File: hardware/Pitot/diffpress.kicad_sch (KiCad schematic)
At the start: 6 parts, among them IC1 ABPMRRV060MG2A3

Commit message: small changes, cubemx needs checking
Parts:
- added R18: 4.7k, Resistor_SMD:R_0603_1608Metric_Pad0.98x0.95mm_HandSolder, symbol Device:R
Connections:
- net GND: now also R18.2
- net pressureERR: now also R18.1
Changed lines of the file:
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@@
 	(paper "A4")
+	(junction
+		(at 90.17 58.42)
+		(diameter 0)
+		(color 0 0 0 0)
+	)
 	(junction
 		(at 101.6 74.93)
@@
 	(wire
 		(pts
+			(xy 90.17 58.42) (xy 90.17 62.23)
+		)
+		(stroke
+			(width 0)
+			(type default)
+		)
+	)
+	(wire
+		(pts
 			(xy 166.37 66.04) (xy 166.37 69.85)
 		)
@@
 	(wire
 		(pts
-			(xy 96.52 58.42) (xy 115.57 58.42)
+			(xy 90.17 58.42) (xy 115.57 58.42)
+		)
+		(stroke
+			(width 0)
+			(type default)
+		)
+	)
+	(wire
+		(pts
+			(xy 81.28 58.42) (xy 90.17 58.42)
 		)
 		(stroke
@@
 		(pts
 			(xy 151.13 69.85) (xy 166.37 69.85)
+		)
+		(stroke
+			(width 0)
+			(type default)
+		)
+	)
+	(wire
+		(pts
+			(xy 90.17 69.85) (xy 90.17 73.66)
 		)
 		(stroke
@@
 	(hierarchical_label "pressureERR"
 		(shape output)
-		(at 96.52 58.42 180)
+		(at 81.28 58.42 180)
 		(effects
 			(font
@@
 					(unit 1)
 				)
+			)
+		)
+	)
+	(symbol
+		(lib_id "power:GND")
+		(at 90.17 73.66 0)
+		(unit 1)
+		(exclude_from_sim no)
+		(in_bom yes)
+		(on_board yes)
+		(dnp no)
+		(property "Reference" "#PWR030"
+			(at 90.17 80.01 0)
+			(effects
+				(font
+					(size 1.27 1.27)
+				)
+				(hide yes)
+			)
+		)
+		(property "Value" "GND"
+			(at 90.17 77.724 0)
+			(effects
+				(font
+					(size 1.27 1.27)
+				)
+			)
+		)
+		(property "Footprint" ""
+			(at 90.17 73.66 0)
+			(effects
+				(font
+					(size 1.27 1.27)
+				)
+				(hide yes)
+			)
+		)
+		(property "Datasheet" ""
+			(at 90.17 73.66 0)
+			(effects
+				(font
+					(size 1.27 1.27)
+				)
+				(hide yes)
+			)
+		)
+		(property "Description" "Power symbol creates a global label with name \"GND\" , ground"
+			(at 90.17 73.66 0)
+			(effects
+				(font
+					(size 1.27 1.27)
+				)
+				(hide yes)
+			)
+		)
+		(pin "1"
+		)
+		(instances
+			(project "Pitot"
+				(path "/b92f2323-f48d-45bc-8bf4-2cff87ecc0bc/1905abd7-6f86-4e5e-9f35-1efc7ddf21d8"
+					(reference "#PWR031")
+					(unit 1)
+				)
+				(path "/b92f2323-f48d-45bc-8bf4-2cff87ecc0bc/5b12aa57-1644-4b30-a37a-ee43545972bc"
+					(reference "#PWR030")
+					(unit 1)
+				)
+			)
+		)
+	)
+	(symbol
+		(lib_id "Device:R")
+		(at 90.17 66.04 0)
+		(unit 1)
+		(exclude_from_sim no)
+		(in_bom yes)
+		(on_board yes)
+		(dnp yes)
+		(property "Reference" "R18"
+			(at 92.202 65.2779 0)
+			(effects
+				(font
+					(size 1.27 1.27)
+				)
+				(justify left)
+			)
+		)
+		(property "Value" "4.7k"
+			(at 92.202 67.564 0)
+			(effects
+				(font
+					(size 1.27 1.27)
+				)
+				(justify left)
+			)
+		)
+		(property "Footprint" "Resistor_SMD:R_0603_1608Metric_Pad0.98x0.95mm_HandSolder"
+			(at 88.392 66.04 90)
+			(effects
+				(font
+					(size 1.27 1.27)
+				)
+				(hide yes)
+			)
+		)
+		(property "Datasheet" "~"
+			(at 90.17 66.04 0)
+			(effects
+				(font
+					(size 1.27 1.27)
+				)
+				(hide yes)
+			)
+		)
+		(property "Description" "Resistor"
+			(at 90.17 66.04 0)
+			(effects
+				(font
+					(size 1.27 1.27)
+				)
+				(hide yes)
+			)
+		)
+		(property "P/N" "71-CRCW0603-4.7K-E3"
+			(at 90.17 66.04 0)
+			(effects
+				(font
+					(size 1.27 1.27)
+				)
+				(hide yes)
+			)
+		)
+		(pin "2"
+		)
+		(pin "1"
+		)
+		(instances
+			(project "Pitot"
+				(path "/b92f2323-f48d-45bc-8bf4-2cff87ecc0bc/1905abd7-6f86-4e5e-9f35-1efc7ddf21d8"
+					(reference "R19")
+					(unit 1)
+				)
+				(path "/b92f2323-f48d-45bc-8bf4-2cff87ecc0bc/5b12aa57-1644-4b30-a37a-ee43545972bc"
+					(reference "R18")
+					(unit 1)
+				)

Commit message: finished layout
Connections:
- net +3.3VMCU is gone; now on net +3.3V: C5.1, C6.1, IC1.2 (VSUPPLY)
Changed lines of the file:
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@@
 			)
 		)
-		(property "Value" "+3.3VMCU"
+		(property "Value" "+3.3V"
 			(at 101.6 60.452 0)
 			(effects

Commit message: final pitot board + bom files
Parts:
- IC1: P/N 785-ABPMRRV060MG2A3 -> ABPMRRV060MG2A3
- R10, R11, R18, R9: P/N 71-CRCW0603-4.7K-E3 -> CRCW06034K70FKEA
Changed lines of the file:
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@@
 			)
 		)
-		(property "P/N" "71-CRCW0603-4.7K-E3"
+		(property "P/N" "CRCW06034K70FKEA"
 			(at 115.57 53.34 0)
 			(effects
@@
 			)
 		)
-		(property "P/N" "71-CRCW0603-4.7K-E3"
+		(property "P/N" "CRCW06034K70FKEA"
 			(at 166.37 62.23 0)
 			(effects
@@
 			)
 		)
-		(property "P/N" "71-CRCW0603-4.7K-E3"
+		(property "P/N" "CRCW06034K70FKEA"
 			(at 90.17 66.04 0)
 			(effects
@@
 			)
 		)
-		(property "P/N" "71-CRCW0603-4.7K-E3"
+		(property "P/N" "CRCW06034K70FKEA"
 			(at 156.21 62.23 0)
 			(effects
@@
 			)
 		)
-		(property "P/N" "785-ABPMRRV060MG2A3"
+		(property "P/N" "ABPMRRV060MG2A3"
 			(at 151.13 69.85 0)
 			(effects

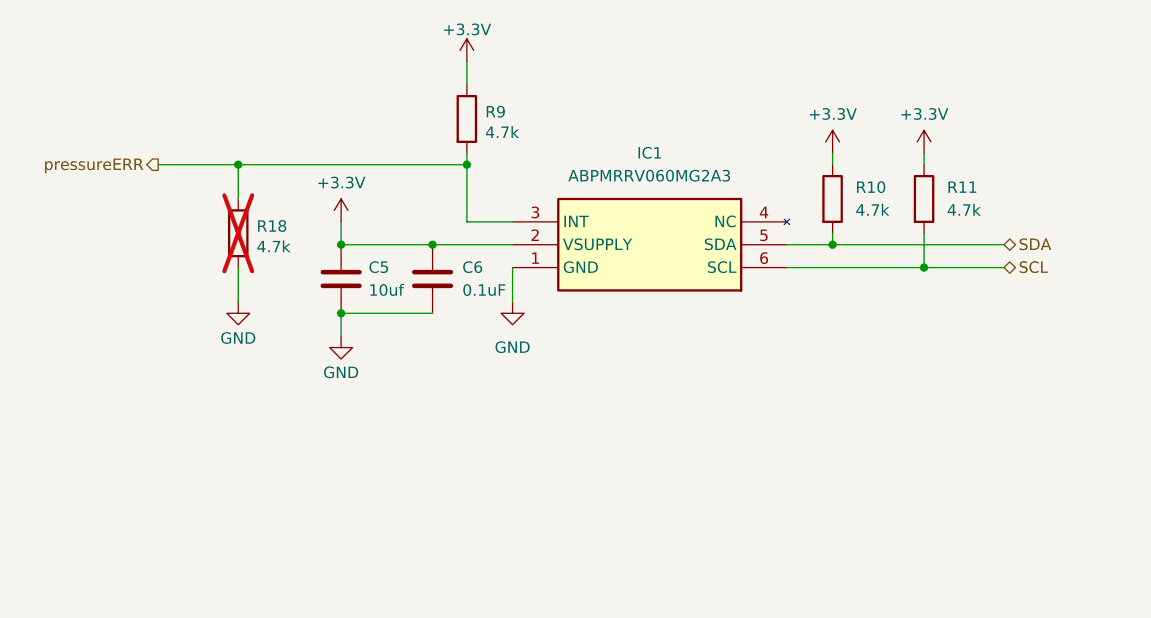
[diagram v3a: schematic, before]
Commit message: Rev B Review (#2)
* schematic changes: ldo switched out of qfn, op amp footprint fixed, resistor array changed. need add correct stm changes

* finished sch + removed LDO

* removed LDO, added correct cube.

* op-amp changes

* layout finished, need to add some more silkscreen + ready for review!

* finished layout + silkscreen, ready to review.

* mac files removed

* made changes from review council

* added 3d models for 01x05 nanofits

* added stepfiles for sus-rh

* sus-rh production ready

* remove .DS_Store files

* fixed nanofit for linpot

* added "validated silkscreen"

* Added jlc assembly files

* pitot board sch review. the biggest change was the switch to nanofits and different pressure sensor

---------

Co-authored-by: Lakshay983 <56173382+Lakshay983@users.noreply.github.com>
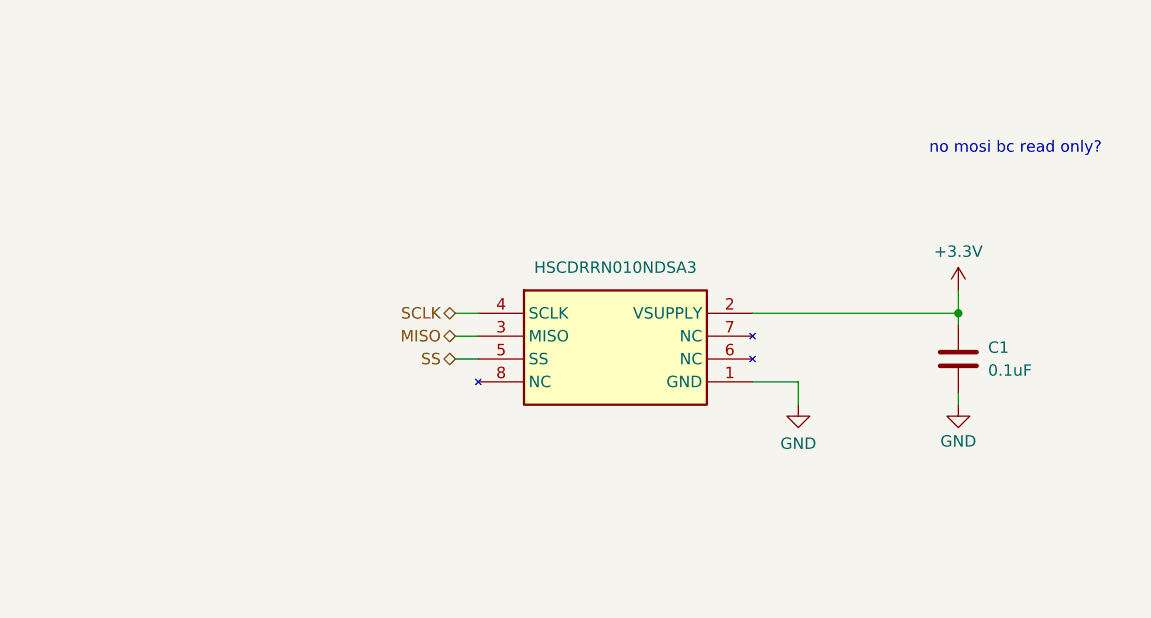
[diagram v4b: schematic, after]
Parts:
- removed C5: 10uf, Capacitor_SMD:C_0805_2012Metric_Pad1.18x1.45mm_HandSolder, symbol Device:C
- removed C6: 0.1uF, Capacitor_SMD:C_0603_1608Metric_Pad1.08x0.95mm_HandSolder, symbol Device:C
- removed IC1: ABPMRRV060MG2A3, footprints:ABPMRRV060MG2A3, symbol ABPMRRV060MG2A3:ABPMRRV060MG2A3
- removed R10, R11, R18, R9: 4.7k, Resistor_SMD:R_0603_1608Metric_Pad0.98x0.95mm_HandSolder, symbol Device:R
- added C1: 0.1uF, Capacitor_SMD:C_0603_1608Metric_Pad1.08x0.95mm_HandSolder, symbol Device:C
- added IC1: HSCDRRN010NDSA3, symbol ABPMRRV060MG2A3:HSCDRRN010NDSA3_Pressure
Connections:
- net +3.3V: now also C1.1, IC1.2 (VSUPPLY)
- net GND: now also C1.2, IC1.1 (GND)
- new net MISO: IC1.3 (MISO)
- new net SCLK: IC1.4 (SCLK)
- new net SS: IC1.5 (SS)
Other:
- note added: "no mosi bc read only?"

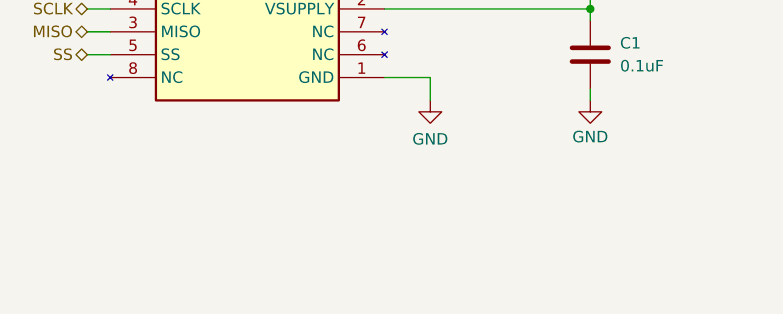
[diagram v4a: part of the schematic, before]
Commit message: Pitot Board Rev B (#3)
* init

* added layout

* ready to review

* finished pitot board

* pitot board ordered, routing+size finished for temperature board so pull??

* finished tempboard silkscreen

* resized temperature board

* poo oo ee

* ughhhhhhhhhhhhhhhhhhghghghhhhhhhhhhhhhhhhhhh

* working i2c on RH board

* cleanup?

* small

* added read me

* fixed mistake

* Fix image filename case in README.md

* Add new line for telemetry components explanation
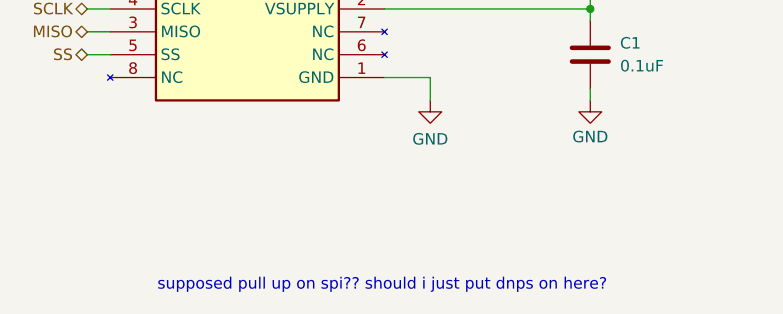
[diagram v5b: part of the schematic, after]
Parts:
- IC1: footprint (none) -> UTSVT_Connectors:HSCDRRN010NDSA3; P/N (none) -> HSCDRRN010NDSA3
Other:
- note added: "supposed pull up on spi?? should i just put dnps on here?"
